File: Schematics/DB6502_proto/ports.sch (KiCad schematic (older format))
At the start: 20 parts, among them J1 Power plug, J10 System Bus, J2 Controls, J3 AVR ISP, J4 Debug USB, J5 JPR, J6 Debug UART, J7 UART A, J8 UART B, J9 I/O Bus

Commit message: Moving things around
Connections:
- net +5V: now also J9.39 (Pin_39)
- net GND: now also J9.40 (Pin_40)
- net LATCH_Q0: now also J9.31 (Pin_31); no longer J9.33 (Pin_33)
- net LATCH_Q1: now also J9.32 (Pin_32); no longer J9.34 (Pin_34)
- net LATCH_Q2: now also J9.33 (Pin_33); no longer J9.35 (Pin_35)
- net LATCH_Q3: now also J9.34 (Pin_34); no longer J9.36 (Pin_36)
- net LATCH_Q4: now also J9.35 (Pin_35); no longer J9.37 (Pin_37)
- net LATCH_Q5: now also J9.36 (Pin_36); no longer J9.38 (Pin_38)
- net LATCH_Q6: now also J9.37 (Pin_37); no longer J9.39 (Pin_39)
- net LATCH_Q7: now also J9.38 (Pin_38); no longer J9.40 (Pin_40)
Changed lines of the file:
@@
 6502_CLK
 Wire Wire Line
-	1350 4600 1350 3800
-Wire Wire Line
-	1350 3800 3050 3800
+	1750 5000 1750 3800
+Wire Wire Line
+	1750 3800 3050 3800
 Text GLabel 1350 2400 1    50   Input ~ 0
 R~W
 Wire Wire Line
-	1200 4600 1200 3700
-Wire Wire Line
-	1200 3700 3050 3700
-Text GLabel 1050 4600 3    50   Input ~ 0
+	1600 5000 1600 3700
+Wire Wire Line
+	1600 3700 3050 3700
+Text GLabel 1450 5000 3    50   Input ~ 0
 ~6502_RES
 Wire Wire Line
-	1050 4600 1050 3600
-Wire Wire Line
-	1050 3600 3050 3600
+	1450 5000 1450 3600
+Wire Wire Line
+	1450 3600 3050 3600
 Text GLabel 6400 7400 2    50   Input ~ 0
 SYNC
@@
 6502_RDY
 Wire Wire Line
-	1500 4600 1500 3900
-Wire Wire Line
-	1500 3900 3050 3900
-Wire Wire Line
-	1650 4600 1650 4000
-Wire Wire Line
-	1650 4000 3050 4000
-Wire Wire Line
-	1800 4600 1800 4100
-Wire Wire Line
-	1800 4100 3050 4100
+	1900 5000 1900 3900
+Wire Wire Line
+	1900 3900 3050 3900
+Wire Wire Line
+	2050 5000 2050 4000
+Wire Wire Line
+	2050 4000 3050 4000
+Wire Wire Line
+	2150 5000 2150 4100
+Wire Wire Line
+	2150 4100 3050 4100
 $Comp
 L Device:R R2
@@
 Wire Wire Line
 	2950 1000 3050 1000
-Text GLabel 1200 4600 3    50   Output ~ 0
+Text GLabel 1600 5000 3    50   Output ~ 0
 ~VIA2_IRQ
-Text GLabel 1350 4600 3    50   Output ~ 0
+Text GLabel 1750 5000 3    50   Output ~ 0
 ~EXT_IRQ
 Wire Wire Line
@@
 Wire Wire Line
 	5700 4200 6850 4200
-Text GLabel 1500 4600 3    50   Output ~ 0
+Text GLabel 1900 5000 3    50   Output ~ 0
 ~NMI
 Text GLabel 6500 1100 1    50   Input ~ 0
@@
 Wire Wire Line
 	8950 2550 9150 2550
-Text GLabel 2950 5000 3    50   Input ~ 0
+Text GLabel 2750 5000 3    50   Input ~ 0
 LATCH_Q7
-Text GLabel 2850 5000 3    50   Input ~ 0
+Text GLabel 2650 5000 3    50   Input ~ 0
 LATCH_Q6
-Text GLabel 2750 5000 3    50   Input ~ 0
+Text GLabel 2550 5000 3    50   Input ~ 0
 LATCH_Q5
-Text GLabel 2650 5000 3    50   Input ~ 0
+Text GLabel 2450 5000 3    50   Input ~ 0
 LATCH_Q4
-Text GLabel 2550 5000 3    50   Input ~ 0
+Text GLabel 2350 5000 3    50   Input ~ 0
 LATCH_Q3
-Text GLabel 2450 5000 3    50   Input ~ 0
+Text GLabel 2250 5000 3    50   Input ~ 0
 LATCH_Q2
-Text GLabel 2350 5000 3    50   Input ~ 0
+Text GLabel 2150 5000 3    50   Input ~ 0
 LATCH_Q1
-Text GLabel 2250 5000 3    50   Input ~ 0
+Text GLabel 2050 5000 3    50   Input ~ 0
 LATCH_Q0
 Wire Wire Line
@@
 Wire Bus Line
 	2300 6700 3800 6700
+Text GLabel 2850 5000 3    50   Input ~ 0
++5V
+Text GLabel 2950 5000 3    50   Input ~ 0
+GND
 $EndSCHEMATC

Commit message: Further improvements
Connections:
- net 6502_RDY: now also J10.25 (Pin_25)
- net RDY_M1F: now also J10.26 (Pin_26)
- net RDY_M2F: now also J10.27 (Pin_27)
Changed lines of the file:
@@
 Text GLabel 2950 5000 3    50   Input ~ 0
 GND
+Text GLabel 4900 6800 3    50   Input ~ 0
+RDY_M1F
+Text GLabel 5000 6800 3    50   Input ~ 0
+RDY_M2F
+Wire Wire Line
+	4800 6800 4800 6400
+Wire Wire Line
+	4900 6800 4900 6400
+Text GLabel 4800 6800 3    50   Input ~ 0
+6502_RDY
+Wire Wire Line
+	5000 6800 5000 6400
 Wire Bus Line
 	10750 2150 10750 2350

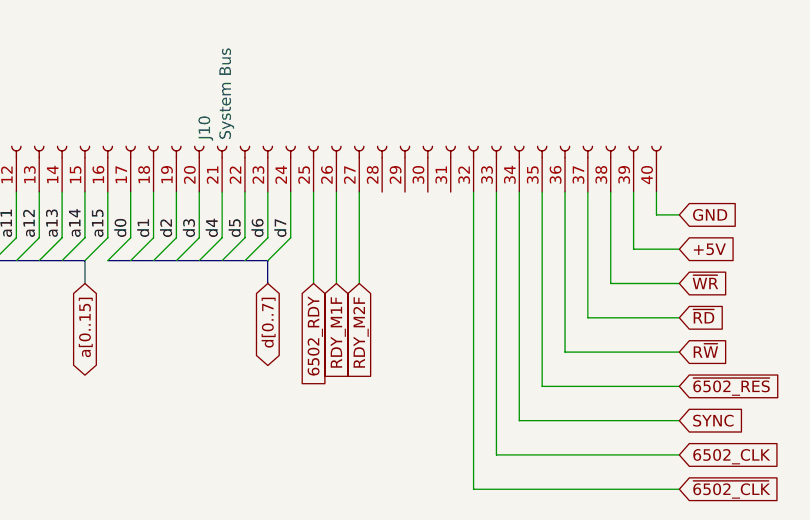
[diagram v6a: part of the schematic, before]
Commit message: Added bus labels
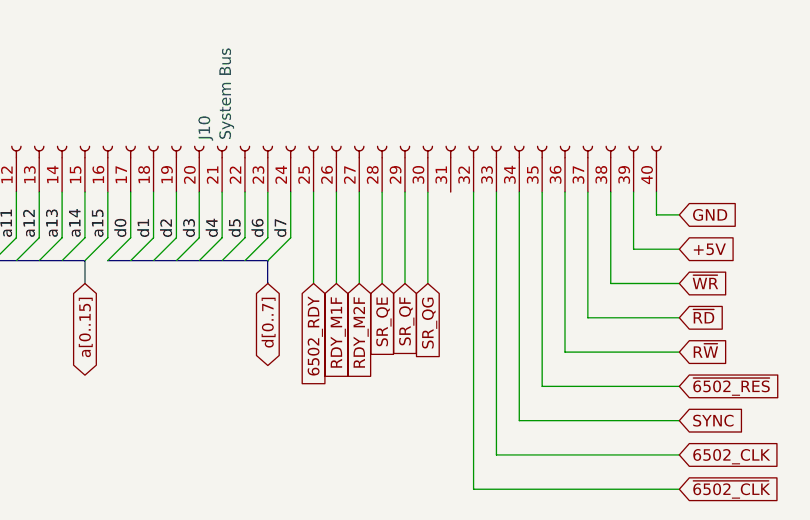
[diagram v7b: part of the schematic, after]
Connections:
- net SR_QE: now reaches J10.28 (Pin_28)
- net SR_QF: now reaches J10.29 (Pin_29)
- net SR_QG: now reaches J10.30 (Pin_30)
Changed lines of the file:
@@
 Wire Wire Line
 	5000 6800 5000 6400
+Text GLabel 5100 6800 3    50   Input ~ 0
+SR_QE
+Text GLabel 5200 6800 3    50   Input ~ 0
+SR_QF
+Text GLabel 5300 6800 3    50   Input ~ 0
+SR_QG
+Wire Wire Line
+	5100 6800 5100 6400
+Wire Wire Line
+	5200 6800 5200 6400
+Wire Wire Line
+	5300 6800 5300 6400
 Wire Bus Line
 	10750 2150 10750 2350

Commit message: Added one last line to the system
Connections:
- net BE: now also J10.31 (Pin_31)
- net CLK_1: now also J2.38 (Pin_38)
- net CLK_2: now also J2.39 (Pin_39)
- net CLK_4: now also J2.40 (Pin_40)
- net EXT_BE: now reaches J2.37 (Pin_37)
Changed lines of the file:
@@
 Wire Wire Line
 	5300 6800 5300 6400
+Text GLabel 6200 5000 3    50   Input ~ 0
+CLK_1
+Text GLabel 6300 5000 3    50   Input ~ 0
+CLK_2
+Text GLabel 6400 5000 3    50   Input ~ 0
+CLK_4
+Wire Wire Line
+	6400 5000 6400 4900
+Wire Wire Line
+	6400 4900 6850 4900
+Wire Wire Line
+	6300 5000 6300 4800
+Wire Wire Line
+	6300 4800 6850 4800
+Wire Wire Line
+	6200 5000 6200 4700
+Wire Wire Line
+	6200 4700 6850 4700
+Wire Wire Line
+	6100 5000 6100 4600
+Wire Wire Line
+	6100 4600 6850 4600
+Text GLabel 6100 5000 3    50   Output ~ 0
+EXT_BE
+Text GLabel 5400 6800 3    50   Input ~ 0
+BE
+Wire Wire Line
+	5400 6800 5400 6400
 Wire Bus Line
 	10750 2150 10750 2350
